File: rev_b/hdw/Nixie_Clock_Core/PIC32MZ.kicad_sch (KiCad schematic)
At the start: 3 parts, among them U1001 PIC32MZ2048EFG100_IPF

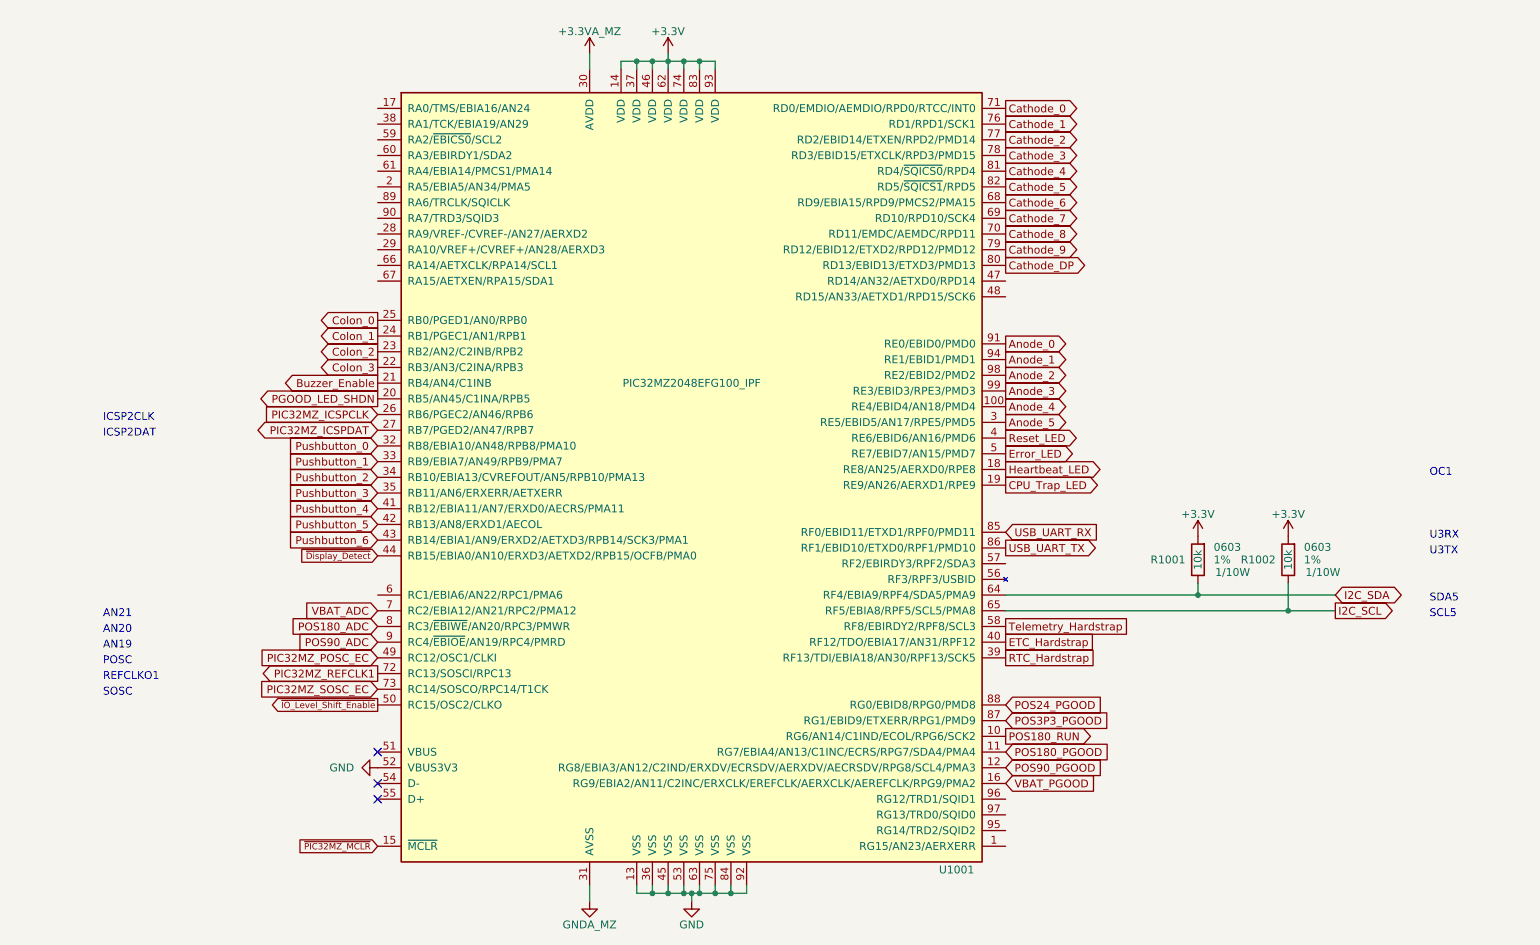
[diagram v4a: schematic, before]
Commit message: routed all IO signals from buffers to PIC
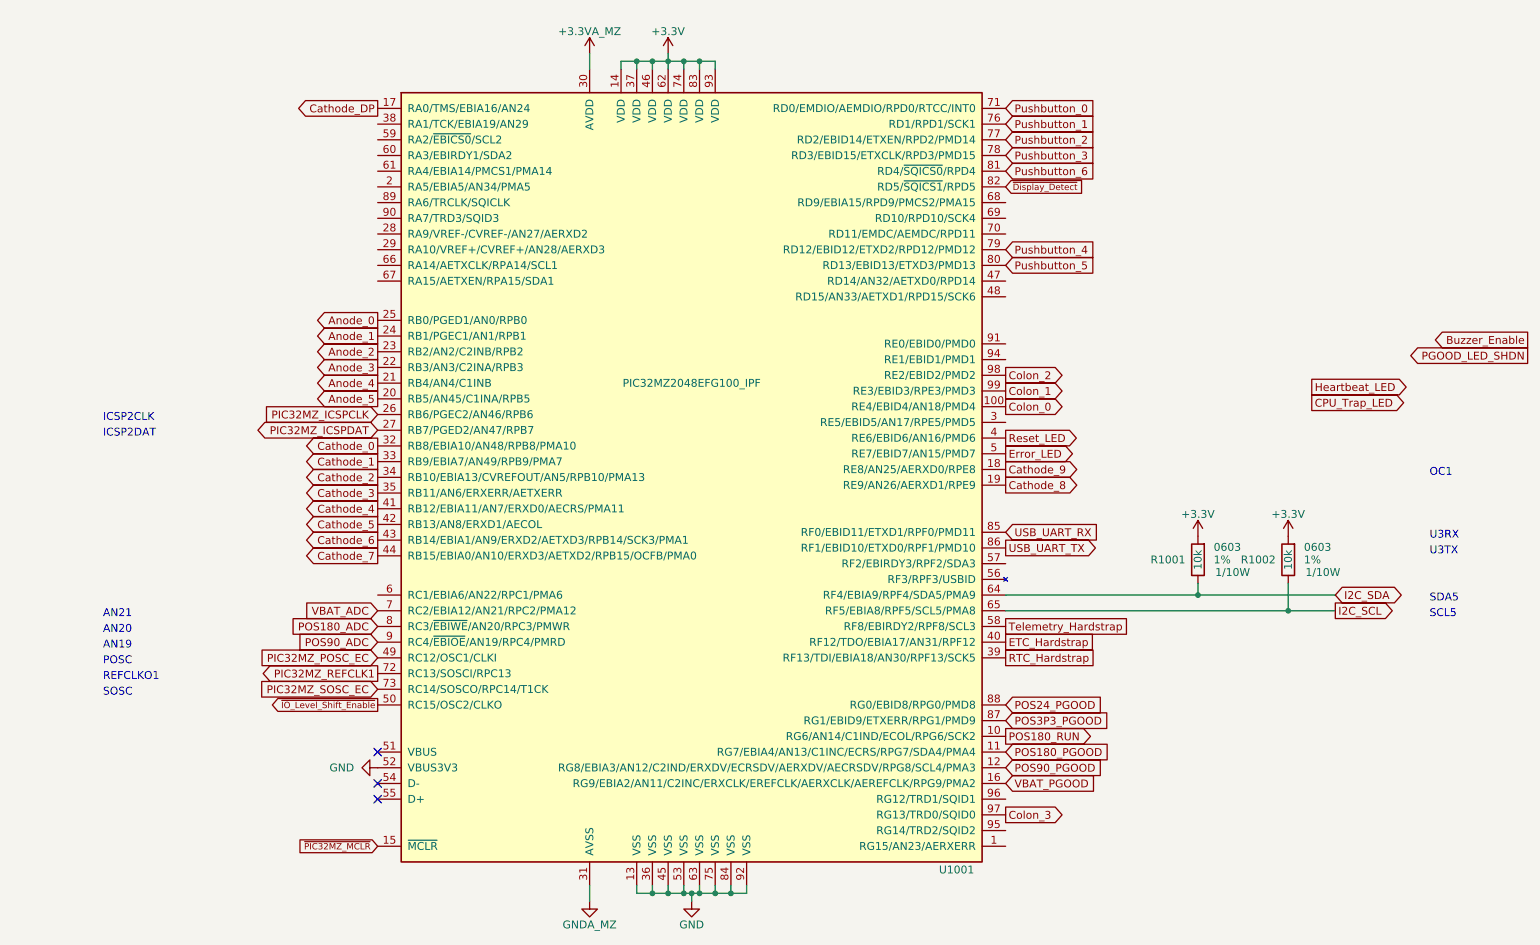
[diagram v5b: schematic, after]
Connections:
- net Anode_0: now also U1001.25 (RB0/PGED1/AN0/RPB0); no longer U1001.91 (RE0/EBID0/PMD0)
- net Anode_1: now also U1001.24 (RB1/PGEC1/AN1/RPB1); no longer U1001.94 (RE1/EBID1/PMD1)
- net Anode_2: now also U1001.23 (RB2/AN2/C2INB/RPB2); no longer U1001.98 (RE2/EBID2/PMD2)
- net Anode_3: now also U1001.22 (RB3/AN3/C2INA/RPB3); no longer U1001.99 (RE3/EBID3/RPE3/PMD3)
- net Anode_4: now also U1001.21 (RB4/AN4/C1INB); no longer U1001.100 (RE4/EBID4/AN18/PMD4)
- net Anode_5: now also U1001.20 (RB5/AN45/C1INA/RPB5); no longer U1001.3 (RE5/EBID5/AN17/RPE5/PMD5)
- net Buzzer_Enable: no longer U1001.21 (RB4/AN4/C1INB)
- net CPU_Trap_LED: no longer U1001.19 (RE9/AN26/AERXD1/RPE9)
- net Cathode_0: now also U1001.32 (RB8/EBIA10/AN48/RPB8/PMA10); no longer U1001.71 (RD0/EMDIO/AEMDIO/RPD0/RTCC/INT0)
- net Cathode_1: now also U1001.33 (RB9/EBIA7/AN49/RPB9/PMA7); no longer U1001.76 (RD1/RPD1/SCK1)
- net Cathode_2: now also U1001.34 (RB10/EBIA13/CVREFOUT/AN5/RPB10/PMA13); no longer U1001.77 (RD2/EBID14/ETXEN/RPD2/PMD14)
- net Cathode_3: now also U1001.35 (RB11/AN6/ERXERR/AETXERR); no longer U1001.78 (RD3/EBID15/ETXCLK/RPD3/PMD15)
- net Cathode_4: now also U1001.41 (RB12/EBIA11/AN7/ERXD0/AECRS/PMA11); no longer U1001.81 (RD4/~{SQICS0}/RPD4)
- net Cathode_5: now also U1001.42 (RB13/AN8/ERXD1/AECOL); no longer U1001.82 (RD5/~{SQICS1}/RPD5)
- net Cathode_6: now also U1001.43 (RB14/EBIA1/AN9/ERXD2/AETXD3/RPB14/SCK3/PMA1); no longer U1001.68 (RD9/EBIA15/RPD9/PMCS2/PMA15)
- net Cathode_7: now also U1001.44 (RB15/EBIA0/AN10/ERXD3/AETXD2/RPB15/OCFB/PMA0); no longer U1001.69 (RD10/RPD10/SCK4)
- net Cathode_8: now also U1001.19 (RE9/AN26/AERXD1/RPE9); no longer U1001.70 (RD11/EMDC/AEMDC/RPD11)
- net Cathode_9: now also U1001.18 (RE8/AN25/AERXD0/RPE8); no longer U1001.79 (RD12/EBID12/ETXD2/RPD12/PMD12)
- net Cathode_DP: now also U1001.17 (RA0/TMS/EBIA16/AN24); no longer U1001.80 (RD13/EBID13/ETXD3/PMD13)
- net Colon_0: now also U1001.100 (RE4/EBID4/AN18/PMD4); no longer U1001.25 (RB0/PGED1/AN0/RPB0)
- net Colon_1: now also U1001.99 (RE3/EBID3/RPE3/PMD3); no longer U1001.24 (RB1/PGEC1/AN1/RPB1)
- net Colon_2: now also U1001.98 (RE2/EBID2/PMD2); no longer U1001.23 (RB2/AN2/C2INB/RPB2)
- net Colon_3: now also U1001.97 (RG13/TRD0/SQID0); no longer U1001.22 (RB3/AN3/C2INA/RPB3)
- net Heartbeat_LED: no longer U1001.18 (RE8/AN25/AERXD0/RPE8)
- net PGOOD_LED_SHDN: no longer U1001.20 (RB5/AN45/C1INA/RPB5)
- net Pushbutton_0: now also U1001.71 (RD0/EMDIO/AEMDIO/RPD0/RTCC/INT0); no longer U1001.32 (RB8/EBIA10/AN48/RPB8/PMA10)
- net Pushbutton_1: now also U1001.76 (RD1/RPD1/SCK1); no longer U1001.33 (RB9/EBIA7/AN49/RPB9/PMA7)
- net Pushbutton_2: now also U1001.77 (RD2/EBID14/ETXEN/RPD2/PMD14); no longer U1001.34 (RB10/EBIA13/CVREFOUT/AN5/RPB10/PMA13)
- net Pushbutton_3: now also U1001.78 (RD3/EBID15/ETXCLK/RPD3/PMD15); no longer U1001.35 (RB11/AN6/ERXERR/AETXERR)
- net Pushbutton_4: now also U1001.79 (RD12/EBID12/ETXD2/RPD12/PMD12); no longer U1001.41 (RB12/EBIA11/AN7/ERXD0/AECRS/PMA11)
- net Pushbutton_5: now also U1001.80 (RD13/EBID13/ETXD3/PMD13); no longer U1001.42 (RB13/AN8/ERXD1/AECOL)
- net Pushbutton_6: now also U1001.81 (RD4/~{SQICS0}/RPD4); no longer U1001.43 (RB14/EBIA1/AN9/ERXD2/AETXD3/RPB14/SCK3/PMA1)
- net ~{Display_Detect}: now also U1001.82 (RD5/~{SQICS1}/RPD5); no longer U1001.44 (RB15/EBIA0/AN10/ERXD3/AETXD2/RPB15/OCFB/PMA0)

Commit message: lots more core board routing
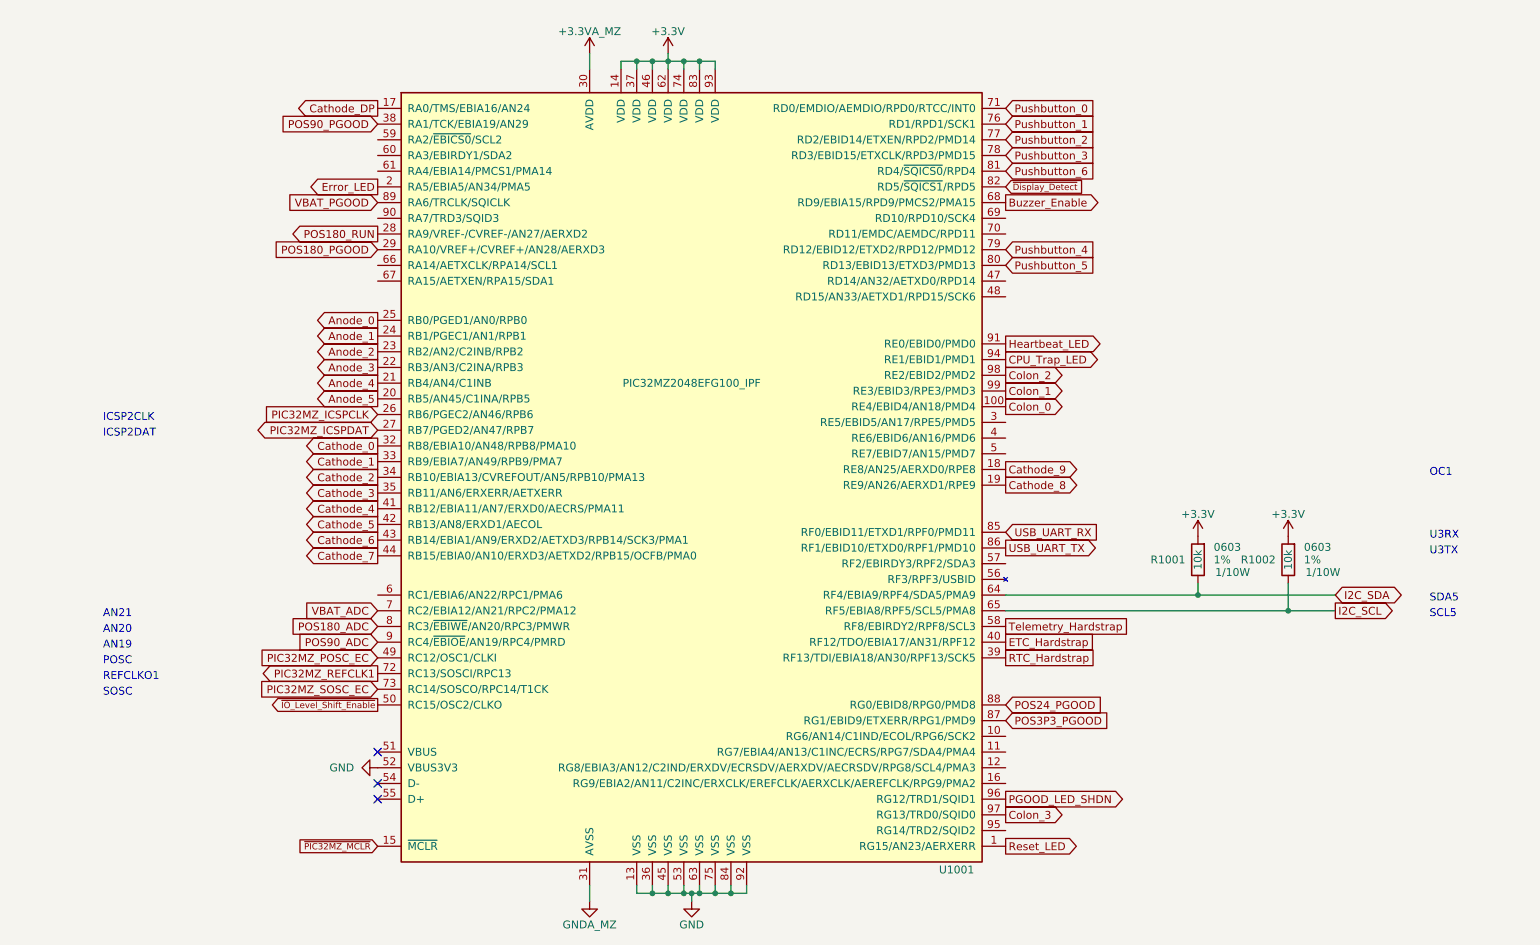
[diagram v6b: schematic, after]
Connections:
- net Buzzer_Enable: now also U1001.68 (RD9/EBIA15/RPD9/PMCS2/PMA15)
- net CPU_Trap_LED: now also U1001.94 (RE1/EBID1/PMD1)
- net Error_LED: now also U1001.2 (RA5/EBIA5/AN34/PMA5); no longer U1001.5 (RE7/EBID7/AN15/PMD7)
- net Heartbeat_LED: now also U1001.91 (RE0/EBID0/PMD0)
- net PGOOD_LED_SHDN: now also U1001.96 (RG12/TRD1/SQID1)
- net POS180_PGOOD: now also U1001.29 (RA10/VREF+/CVREF+/AN28/AERXD3); no longer U1001.11 (RG7/EBIA4/AN13/C1INC/ECRS/RPG7/SDA4/PMA4)
- net POS180_RUN: now also U1001.28 (RA9/VREF-/CVREF-/AN27/AERXD2); no longer U1001.10 (RG6/AN14/C1IND/ECOL/RPG6/SCK2)
- net POS90_PGOOD: now also U1001.38 (RA1/TCK/EBIA19/AN29); no longer U1001.12 (RG8/EBIA3/AN12/C2IND/ERXDV/ECRSDV/AERXDV/AECRSDV/RPG8/SCL4/PMA3)
- net Reset_LED: now also U1001.1 (RG15/AN23/AERXERR); no longer U1001.4 (RE6/EBID6/AN16/PMD6)
- net VBAT_PGOOD: now also U1001.89 (RA6/TRCLK/SQICLK); no longer U1001.16 (RG9/EBIA2/AN11/C2INC/ERXCLK/EREFCLK/AERXCLK/AEREFCLK/RPG9/PMA2)
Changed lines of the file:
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@@
     )
   )
-  (global_label "Buzzer_Enable" (shape output) (at 259.08 70.485 180)
-    (effects (font (size 1.27 1.27)) (justify right))
-    (property "Intersheetrefs" "${INTERSHEET_REFS}" (at 259.08 70.485 0)
+  (global_label "Buzzer_Enable" (shape output) (at 174.625 48.26 0)
+    (effects (font (size 1.27 1.27)) (justify left))
+    (property "Intersheetrefs" "${INTERSHEET_REFS}" (at 174.625 48.26 0)
       (effects (font (size 1.27 1.27)) hide)
     )
@@
     )
   )
-  (global_label "Reset_LED" (shape output) (at 174.625 86.36 0)
-    (effects (font (size 1.27 1.27)) (justify left))
-    (property "Intersheetrefs" "${INTERSHEET_REFS}" (at 174.625 86.36 0)
+  (global_label "Reset_LED" (shape output) (at 174.625 152.4 0)
+    (effects (font (size 1.27 1.27)) (justify left))
+    (property "Intersheetrefs" "${INTERSHEET_REFS}" (at 174.625 152.4 0)
       (effects (font (size 1.27 1.27)) hide)
     )
@@
     )
   )
-  (global_label "POS180_RUN" (shape output) (at 174.625 134.62 0)
-    (effects (font (size 1.27 1.27)) (justify left))
-    (property "Intersheetrefs" "${INTERSHEET_REFS}" (at 174.625 134.62 0)
+  (global_label "POS180_RUN" (shape output) (at 73.025 53.34 180)
+    (effects (font (size 1.27 1.27)) (justify right))
+    (property "Intersheetrefs" "${INTERSHEET_REFS}" (at 73.025 53.34 0)
       (effects (font (size 1.27 1.27)) hide)
     )
@@
     )
   )
-  (global_label "Error_LED" (shape output) (at 174.625 88.9 0)
-    (effects (font (size 1.27 1.27)) (justify left))
-    (property "Intersheetrefs" "${INTERSHEET_REFS}" (at 174.625 88.9 0)
+  (global_label "Error_LED" (shape output) (at 73.025 45.72 180)
+    (effects (font (size 1.27 1.27)) (justify right))
+    (property "Intersheetrefs" "${INTERSHEET_REFS}" (at 73.025 45.72 0)
       (effects (font (size 1.27 1.27)) hide)
     )
@@
     )
   )
-  (global_label "POS180_PGOOD" (shape input) (at 174.625 137.16 0)
-    (effects (font (size 1.27 1.27)) (justify left))
-    (property "Intersheetrefs" "${INTERSHEET_REFS}" (at 174.625 137.16 0)
+  (global_label "POS180_PGOOD" (shape input) (at 73.025 55.88 180)
+    (effects (font (size 1.27 1.27)) (justify right))
+    (property "Intersheetrefs" "${INTERSHEET_REFS}" (at 73.025 55.88 0)
       (effects (font (size 1.27 1.27)) hide)
     )
@@
     )
   )
-  (global_label "PGOOD_LED_SHDN" (shape output) (at 259.08 73.025 180)
-    (effects (font (size 1.27 1.27)) (justify right))
-    (property "Intersheetrefs" "${INTERSHEET_REFS}" (at 259.08 73.025 0)
-      (effects (font (size 1.27 1.27)) hide)
-    )
-  )
-  (global_label "CPU_Trap_LED" (shape output) (at 224.155 80.645 0)
-    (effects (font (size 1.27 1.27)) (justify left))
-    (property "Intersheetrefs" "${INTERSHEET_REFS}" (at 224.155 80.645 0)
+  (global_label "PGOOD_LED_SHDN" (shape output) (at 174.625 144.78 0)
+    (effects (font (size 1.27 1.27)) (justify left))
+    (property "Intersheetrefs" "${INTERSHEET_REFS}" (at 174.625 144.78 0)
+      (effects (font (size 1.27 1.27)) hide)
+    )
+  )
+  (global_label "CPU_Trap_LED" (shape output) (at 174.625 73.66 0)
+    (effects (font (size 1.27 1.27)) (justify left))
+    (property "Intersheetrefs" "${INTERSHEET_REFS}" (at 174.625 73.66 0)
       (effects (font (size 1.27 1.27)) hide)
     )
@@
     )
   )
-  (global_label "POS90_PGOOD" (shape input) (at 174.625 139.7 0)
-    (effects (font (size 1.27 1.27)) (justify left))
-    (property "Intersheetrefs" "${INTERSHEET_REFS}" (at 174.625 139.7 0)
+  (global_label "POS90_PGOOD" (shape input) (at 73.025 35.56 180)
+    (effects (font (size 1.27 1.27)) (justify right))
+    (property "Intersheetrefs" "${INTERSHEET_REFS}" (at 73.025 35.56 0)
       (effects (font (size 1.27 1.27)) hide)
     )
@@
     )
   )
-  (global_label "Heartbeat_LED" (shape output) (at 224.155 78.105 0)
-    (effects (font (size 1.27 1.27)) (justify left))
-    (property "Intersheetrefs" "${INTERSHEET_REFS}" (at 224.155 78.105 0)
+  (global_label "Heartbeat_LED" (shape output) (at 174.625 71.12 0)
+    (effects (font (size 1.27 1.27)) (justify left))
+    (property "Intersheetrefs" "${INTERSHEET_REFS}" (at 174.625 71.12 0)
       (effects (font (size 1.27 1.27)) hide)
     )
@@
     )
   )
-  (global_label "VBAT_PGOOD" (shape input) (at 174.625 142.24 0)
-    (effects (font (size 1.27 1.27)) (justify left))
-    (property "Intersheetrefs" "${INTERSHEET_REFS}" (at 174.625 142.24 0)
-      (effects (font (size 1.27 1.27)) hide)
-    )
+  (global_label "VBAT_PGOOD" (shape input) (at 73.025 48.26 180)
+    (effects (font (size 1.27 1.27)) (justify right))
+    (property "Intersheetrefs" "${INTERSHEET_REFS}" (at 73.025 48.26 0)
+      (effects (font (size 1.27 1.27)) hide)
+    )

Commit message: got to 0 unconnects
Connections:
- net VBAT_PGOOD: now also U1001.48 (RD15/AN33/AETXD1/RPD15/SCK6); no longer U1001.89 (RA6/TRCLK/SQICLK)
- net ~{IO_Level_Shift_Enable}: now also U1001.90 (RA7/TRD3/SQID3); no longer U1001.50 (RC15/OSC2/CLKO)
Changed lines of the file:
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@@
     )
   )
-  (global_label "~{IO_Level_Shift_Enable}" (shape output) (at 73.025 129.54 180)
+  (global_label "~{IO_Level_Shift_Enable}" (shape output) (at 73.025 50.8 180)
     (effects (font (size 1.016 1.016)) (justify right))
-    (property "Intersheetrefs" "${INTERSHEET_REFS}" (at 73.025 129.54 0)
+    (property "Intersheetrefs" "${INTERSHEET_REFS}" (at 73.025 50.8 0)
       (effects (font (size 1.27 1.27)) hide)
     )
@@
     )
   )
-  (global_label "VBAT_PGOOD" (shape input) (at 73.025 48.26 180)
-    (effects (font (size 1.27 1.27)) (justify right))
-    (property "Intersheetrefs" "${INTERSHEET_REFS}" (at 73.025 48.26 0)
-      (effects (font (size 1.27 1.27)) hide)
-    )
+  (global_label "VBAT_PGOOD" (shape input) (at 174.625 63.5 0)
+    (effects (font (size 1.27 1.27)) (justify left))
+    (property "Intersheetrefs" "${INTERSHEET_REFS}" (at 174.625 63.5 0)
+      (effects (font (size 1.27 1.27)) hide)
+    )
